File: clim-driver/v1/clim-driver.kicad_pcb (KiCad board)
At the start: 2 copper layers, 60 x 40 mm, 14 parts, among them J1 Conn_01x03_Male, J2 Screw_Terminal_01x02, J3 Conn_01x02_Pin, Q1 BSS138, U1 WeMos_D1_mini

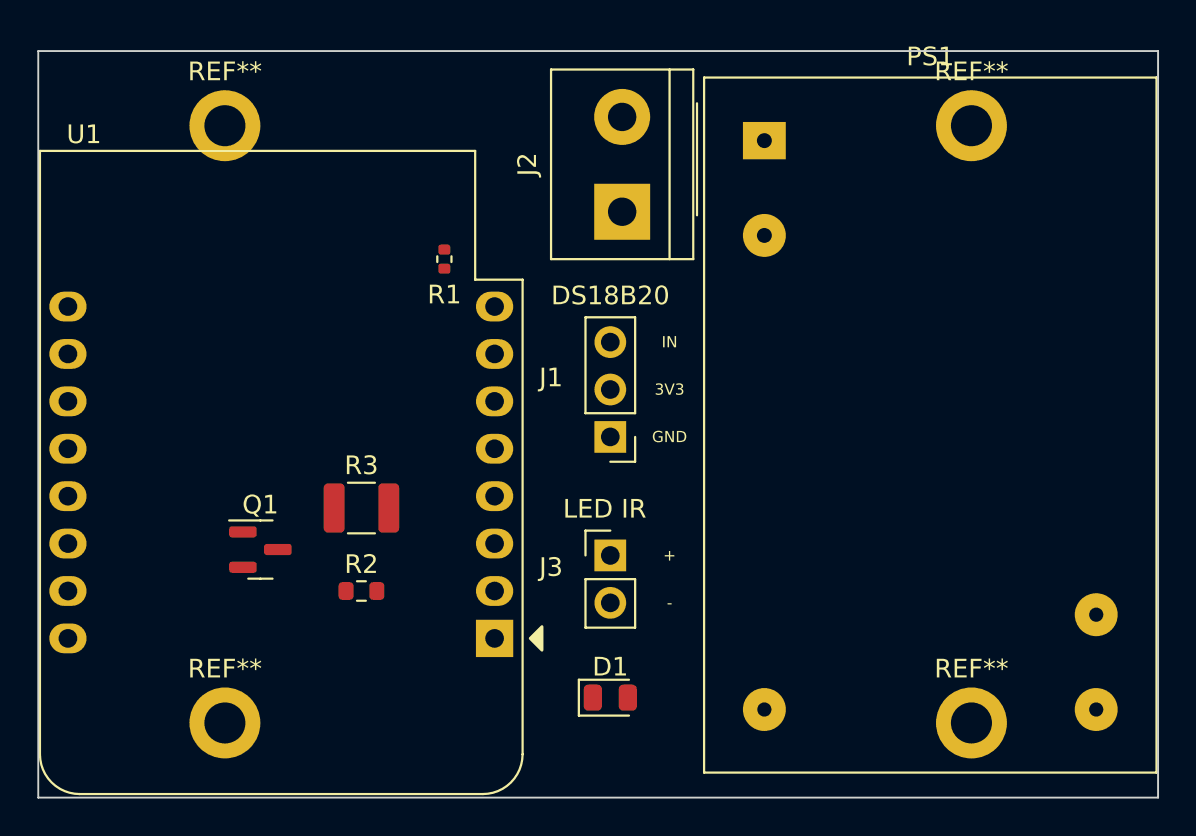
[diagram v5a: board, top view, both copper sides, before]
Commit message: clim driver routing
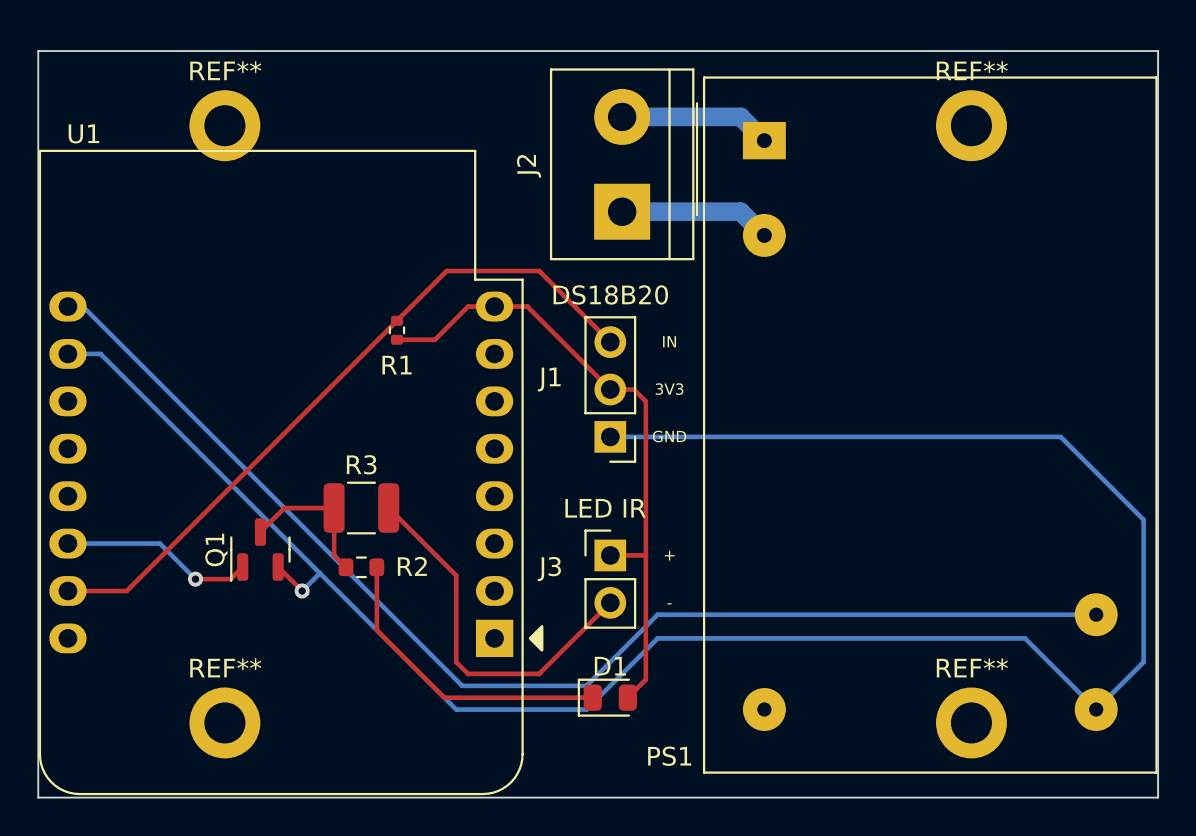
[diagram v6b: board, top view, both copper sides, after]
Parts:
- moved R1 4.58 mm to (109.2, 61.0)
- moved R2 1.27 mm to (107.3, 73.7)
- turned Q1 to 90 degrees
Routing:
- net GND: track 0.00 -> 110.9 mm, vias 0 -> 1
- net +5V: track 0.00 -> 65.1 mm
- net Net-(J1-Pin_3): track 0.00 -> 37.7 mm
- net +3V3: track 0.00 -> 34.4 mm
- net Net-(J3-Pin_2): track 0.00 -> 19.8 mm
- net Net-(D1-K): track 0.00 -> 16.4 mm
- net Net-(Q1-G): track 0.00 -> 10.4 mm, vias 0 -> 1
- net NEUT: track 0.00 -> 8.15 mm
- net LINE: track 0.00 -> 8.15 mm
- net Net-(Q1-D): track 0.00 -> 7.92 mm
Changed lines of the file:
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@@
   )
   (footprint "Resistor_SMD:R_0603_1608Metric" (layer "F.Cu")
-    (at 107.315 74.93)
+    (at 107.315 73.66)
     (descr "Resistor SMD 0603 (1608 Metric), square (rectangular) end terminal, IPC_7351 nominal, (Body size source: IPC-SM-782 page 72, https://www.pcb-3d.com/wordpress/wp-content/uploads/ipc-sm-782a_amendment_1_and_2.pdf), generated with kicad-footprint-generator")
     (tags "resistor")
@@
     (property "ki_keywords" "R res resistor")
     (attr smd)
-    (fp_text reference "R2" (at 0 -1.43) (layer "F.SilkS")
+    (fp_text reference "R2" (at 2.73 0) (layer "F.SilkS")
         (effects (font (size 1 1) (thickness 0.15)))
     )
@@
   )
   (footprint "Package_TO_SOT_SMD:SOT-23" (layer "F.Cu")
-    (at 101.9025 72.71)
+    (at 101.9025 72.71 90)
     (descr "SOT, 3 Pin (https://www.jedec.org/system/files/docs/to-236h.pdf variant AB), generated with kicad-footprint-generator ipc_gullwing_generator.py")
     (tags "SOT TO_SOT_SMD")
@@
     (property "ki_keywords" "N-Channel MOSFET")
     (attr smd)
-    (fp_text reference "Q1" (at 0 -2.4) (layer "F.SilkS")
-        (effects (font (size 1 1) (thickness 0.15)))
-    )
-    (fp_text value "BSS138" (at 0 2.4) (layer "F.Fab")
-        (effects (font (size 1 1) (thickness 0.15)))
-    )
-    (fp_text user "${REFERENCE}" (at 0 0) (layer "F.Fab")
+    (fp_text reference "Q1" (at 0 -2.4 90) (layer "F.SilkS")
+        (effects (font (size 1 1) (thickness 0.15)))
+    )
+    (fp_text value "BSS138" (at 0 2.4 90) (layer "F.Fab")
+        (effects (font (size 1 1) (thickness 0.15)))
+    )
+    (fp_text user "${REFERENCE}" (at 0 0 90) (layer "F.Fab")
         (effects (font (size 0.32 0.32) (thickness 0.05)))
     )
@@
     (fp_line (start 0.65 1.45) (end -0.65 1.45)
       (stroke (width 0.1) (type solid)) (layer "F.Fab"))
-    (pad "1" smd roundrect (at -0.9375 -0.95) (size 1.475 0.6) (layers "F.Cu" "F.Paste" "F.Mask") (roundrect_rratio 0.25)
+    (pad "1" smd roundrect (at -0.9375 -0.95 90) (size 1.475 0.6) (layers "F.Cu" "F.Paste" "F.Mask") (roundrect_rratio 0.25)
       (net 7 "Net-(Q1-G)") (pinfunction "G") (pintype "input"))
-    (pad "2" smd roundrect (at -0.9375 0.95) (size 1.475 0.6) (layers "F.Cu" "F.Paste" "F.Mask") (roundrect_rratio 0.25)
+    (pad "2" smd roundrect (at -0.9375 0.95 90) (size 1.475 0.6) (layers "F.Cu" "F.Paste" "F.Mask") (roundrect_rratio 0.25)
       (net 1 "GND") (pinfunction "S") (pintype "passive"))
-    (pad "3" smd roundrect (at 0.9375 0) (size 1.475 0.6) (layers "F.Cu" "F.Paste" "F.Mask") (roundrect_rratio 0.25)
+    (pad "3" smd roundrect (at 0.9375 0 90) (size 1.475 0.6) (layers "F.Cu" "F.Paste" "F.Mask") (roundrect_rratio 0.25)
       (net 8 "Net-(Q1-D)") (pinfunction "D") (pintype "passive"))
     (model "${KICAD6_3DMODEL_DIR}/Package_TO_SOT_SMD.3dshapes/SOT-23.wrl"
@@
     (property "ki_keywords" "Miniature Module-type Power Supply MeanWell")
     (attr through_hole)
-    (fp_text reference "PS1" (at 8.89 -4.5) (layer "F.SilkS")
+    (fp_text reference "PS1" (at -5.08 33.02) (layer "F.SilkS")
         (effects (font (size 1 1) (thickness 0.15)))
     )
@@
   )
   (footprint "Resistor_SMD:R_0402_1005Metric" (layer "F.Cu")
-    (at 111.76 57.15 90)
+    (at 109.22 60.96 90)
     (descr "Resistor SMD 0402 (1005 Metric), square (rectangular) end terminal, IPC_7351 nominal, (Body size source: IPC-SM-782 page 72, https://www.pcb-3d.com/wordpress/wp-content/uploads/ipc-sm-782a_amendment_1_and_2.pdf), generated with kicad-footprint-generator")
     (tags "resistor")
@@
     (effects (font (size 0.6 0.6) (thickness 0.125)))
   )
+  (segment (start 102.8575 73.6475) (end 104.14 74.93) (width 0.25) (layer "F.Cu") (net 1))
+  (segment (start 102.8525 73.6475) (end 102.8575 73.6475) (width 0.25) (layer "F.Cu") (net 1))
+  (via (at 104.14 74.93) (size 0.8) (drill 0.4) (layers "F.Cu" "B.Cu") (net 1))
+  (segment (start 146.685 81.28) (end 149.225 78.74) (width 0.25) (layer "B.Cu") (net 1))
+  (segment (start 123.19 77.47) (end 119.38 81.28) (width 0.25) (layer "B.Cu") (net 1))
+  (segment (start 144.78 66.675) (end 149.225 71.12) (width 0.25) (layer "B.Cu") (net 1))
+  (segment (start 105.0925 73.9775) (end 112.395 81.28) (width 0.25) (layer "B.Cu") (net 1))
+  (segment (start 142.875 77.47) (end 123.19 77.47) (width 0.25) (layer "B.Cu") (net 1))
+  (segment (start 93.345 62.23) (end 91.59 62.23) (width 0.25) (layer "B.Cu") (net 1))
+  (segment (start 119.38 81.28) (end 112.395 81.28) (width 0.25) (layer "B.Cu") (net 1))
+  (segment (start 120.65 66.675) (end 144.78 66.675) (width 0.25) (layer "B.Cu") (net 1))
+  (segment (start 104.14 74.93) (end 105.0925 73.9775) (width 0.25) (layer "B.Cu") (net 1))
+  (segment (start 105.0925 73.9775) (end 93.345 62.23) (width 0.25) (layer "B.Cu") (net 1))
+  (segment (start 149.225 71.12) (end 149.225 78.74) (width 0.25) (layer "B.Cu") (net 1))
+  (segment (start 146.685 81.28) (end 142.875 77.47) (width 0.25) (layer "B.Cu") (net 1))
+  (segment (start 92.3925 59.69) (end 91.59 59.69) (width 0.25) (layer "B.Cu") (net 2))
+  (segment (start 123.19 76.2) (end 119.38 80.01) (width 0.25) (layer "B.Cu") (net 2))
+  (segment (start 119.38 80.01) (end 112.7125 80.01) (width 0.25) (layer "B.Cu") (net 2))
+  (segment (start 146.685 76.2) (end 123.19 76.2) (width 0.25) (layer "B.Cu") (net 2))
+  (segment (start 112.7125 80.01) (end 92.3925 59.69) (width 0.25) (layer "B.Cu") (net 2))
+  (segment (start 116.205 59.69) (end 120.65 64.135) (width 0.25) (layer "F.Cu") (net 3))
+  (segment (start 109.22 61.47) (end 111.25 61.47) (width 0.25) (layer "F.Cu") (net 3))
+  (segment (start 122.555 73.025) (end 122.555 79.6775) (width 0.25) (layer "F.Cu") (net 3))
+  (segment (start 122.555 64.77) (end 122.555 73.025) (width 0.25) (layer "F.Cu") (net 3))
+  (segment (start 120.65 73.025) (end 122.555 73.025) (width 0.25) (layer "F.Cu") (net 3))
+  (segment (start 113.03 59.69) (end 114.45 59.69) (width 0.25) (layer "F.Cu") (net 3))
+  (segment (start 111.25 61.47) (end 113.03 59.69) (width 0.25) (layer "F.Cu") (net 3))
+  (segment (start 120.65 64.135) (end 121.92 64.135) (width 0.25) (layer "F.Cu") (net 3))
+  (segment (start 121.92 64.135) (end 122.555 64.77) (width 0.25) (layer "F.Cu") (net 3))
+  (segment (start 114.45 59.69) (end 116.205 59.69) (width 0.25) (layer "F.Cu") (net 3))
+  (segment (start 122.555 79.6775) (end 121.5875 80.645) (width 0.25) (layer "F.Cu") (net 3))
+  (segment (start 127.635 49.53) (end 128.905 50.8) (width 1) (layer "B.Cu") (net 4))
+  (segment (start 121.285 49.53) (end 127.635 49.53) (width 1) (layer "B.Cu") (net 4))
+  (segment (start 121.285 54.61) (end 127.635 54.61) (width 1) (layer "B.Cu") (net 5))
+  (segment (start 127.635 54.61) (end 128.905 55.88) (width 1) (layer "B.Cu") (net 5))
+  (segment (start 100.305 74.295) (end 100.9525 73.6475) (width 0.25) (layer "F.Cu") (net 7))
+  (segment (start 98.425 74.295) (end 100.305 74.295) (width 0.25) (layer "F.Cu") (net 7))
+  (via (at 98.425 74.295) (size 0.8) (drill 0.4) (layers "F.Cu" "B.Cu") (net 7))
+  (segment (start 91.59 72.39) (end 96.52 72.39) (width 0.25) (layer "B.Cu") (net 7))
+  (segment (start 96.52 72.39) (end 98.425 74.295) (width 0.25) (layer "B.Cu") (net 7))
+  (segment (start 105.8525 70.485) (end 103.19 70.485) (width 0.25) (layer "F.Cu") (net 8))
+  (segment (start 103.19 70.485) (end 101.9025 71.7725) (width 0.25) (layer "F.Cu") (net 8))
+  (segment (start 105.8525 70.485) (end 105.8525 73.0225) (width 0.25) (layer "F.Cu") (net 8))
+  (segment (start 105.8525 73.0225) (end 106.49 73.66) (width 0.25) (layer "F.Cu") (net 8))
+  (segment (start 120.65 61.595) (end 116.84 57.785) (width 0.25) (layer "F.Cu") (net 9))
+  (segment (start 111.885 57.785) (end 109.22 60.45) (width 0.25) (layer "F.Cu") (net 9))
+  (segment (start 109.22 60.45) (end 94.74 74.93) (width 0.25) (layer "F.Cu") (net 9))
+  (segment (start 94.74 74.93) (end 91.59 74.93) (width 0.25) (layer "F.Cu") (net 9))
+  (segment (start 116.84 57.785) (end 111.885 57.785) (width 0.25) (layer "F.Cu") (net 9))
+  (segment (start 119.7125 80.645) (end 111.76 80.645) (width 0.25) (layer "F.Cu") (net 10))
+  (segment (start 111.76 80.645) (end 108.14 77.025) (width 0.25) (layer "F.Cu") (net 10))
+  (segment (start 108.14 77.025) (end 108.14 73.66) (width 0.25) (layer "F.Cu") (net 10))
+  (segment (start 112.395 74.1025) (end 108.7775 70.485) (width 0.25) (layer "F.Cu") (net 11))
+  (segment (start 112.395 78.74) (end 112.395 74.1025) (width 0.25) (layer "F.Cu") (net 11))
+  (segment (start 116.84 79.375) (end 113.03 79.375) (width 0.25) (layer "F.Cu") (net 11))
+  (segment (start 120.65 75.565) (end 116.84 79.375) (width 0.25) (layer "F.Cu") (net 11))
+  (segment (start 113.03 79.375) (end 112.395 78.74) (width 0.25) (layer "F.Cu") (net 11))
   (group "" locked (id d43d666a-10bd-47fa-a783-07e68fd1da55)
     (members
